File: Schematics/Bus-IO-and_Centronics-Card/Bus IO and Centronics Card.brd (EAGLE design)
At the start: 122.5 x 88.6 mm, 22 parts, among them IC1 W65C22S, IC2 74LS245N, IC3 7416N, X1 RJ45-8X

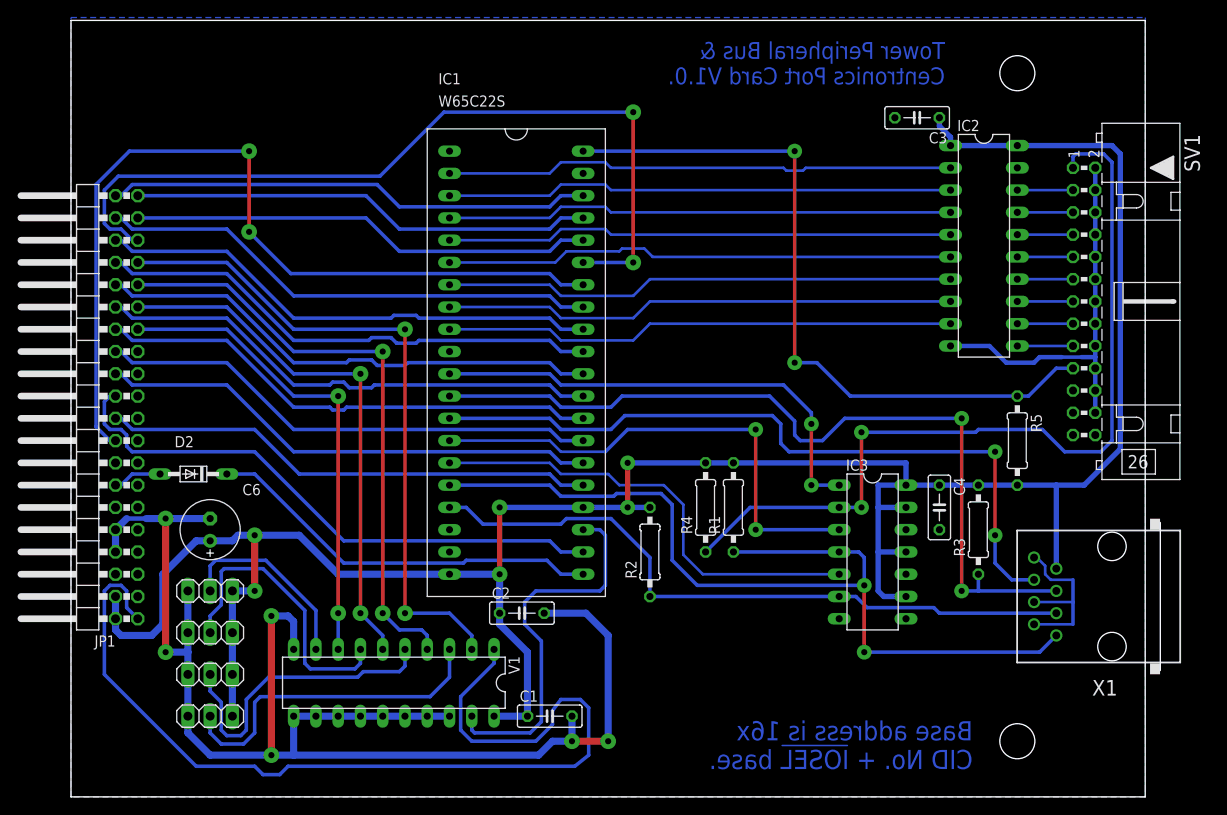
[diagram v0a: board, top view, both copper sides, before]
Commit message: Updated to have a formal Timer IRQ.  Currently this is T1 on the W65C22 on the GPIO card, so if you want to use it that card must be present.
The prebuilt ROM ToEVID.bin uses this card at 0xC040.

A couple of minor whoopsies have been fixed as well.
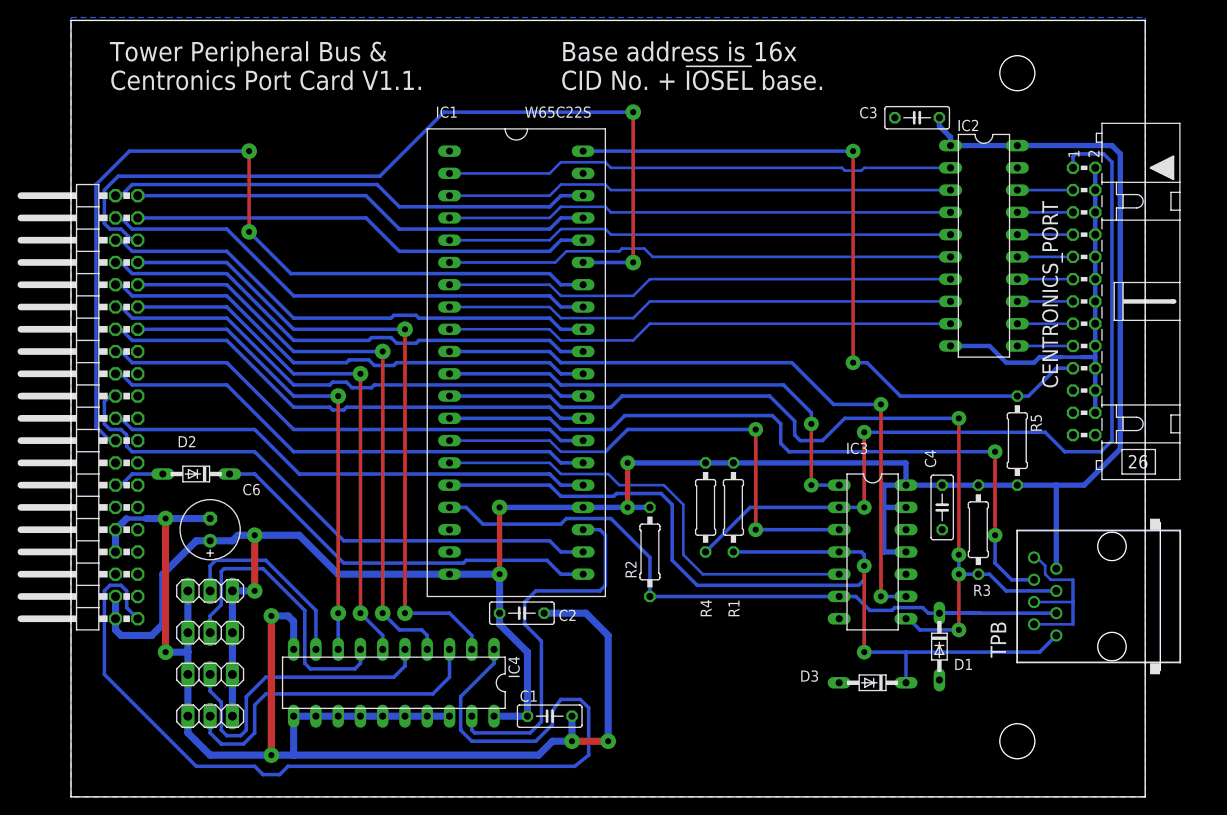
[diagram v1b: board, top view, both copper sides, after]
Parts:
- added D1, D3: BAT85, diode:DO34-7
- moved D2 0.32 mm to (14.3, 36.8)
- moved C4 0.32 mm to (99.4, 33.0)
- renumbered SV1 to CENTRONICS_PORT, V1 to IC4, X1 to TPB
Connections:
- net PB3_TPB_RESET renamed PB3_TPB_SELECT
- new net PB0_ATN_OUT: IC1.PB0, IC3.9
- net GND: now also D1.A, D3.A
- net PB2_TPB_ATN: now also IC3.8
- net PB6_TPB_CLK: now also D3.C
- net PB7_TPB_DATA: now also D1.C
- net VCC: no longer IC3.9
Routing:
- net PB0_ATN_OUT: track 0.00 -> 76.5 mm, vias 0 -> 2
- net PB2_TPB_ATN: track 95.9 -> 105.8 mm, vias 2 -> 4
- net VCC: track 284.3 -> 274.5 mm
- net PB6_TPB_CLK: track 104.7 -> 110.2 mm
- net PB7_TPB_DATA: track 77.3 -> 82.4 mm
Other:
- board text added: "Tower Peripheral Bus & Centronics Port Card V1.1."
- board text removed: "Tower Peripheral Bus & Centronics Port Card V1.0."
